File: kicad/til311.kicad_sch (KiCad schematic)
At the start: 32 parts, among them J1 CONN_1x05, J2 CONN_2x07, U1 PIC16F13145

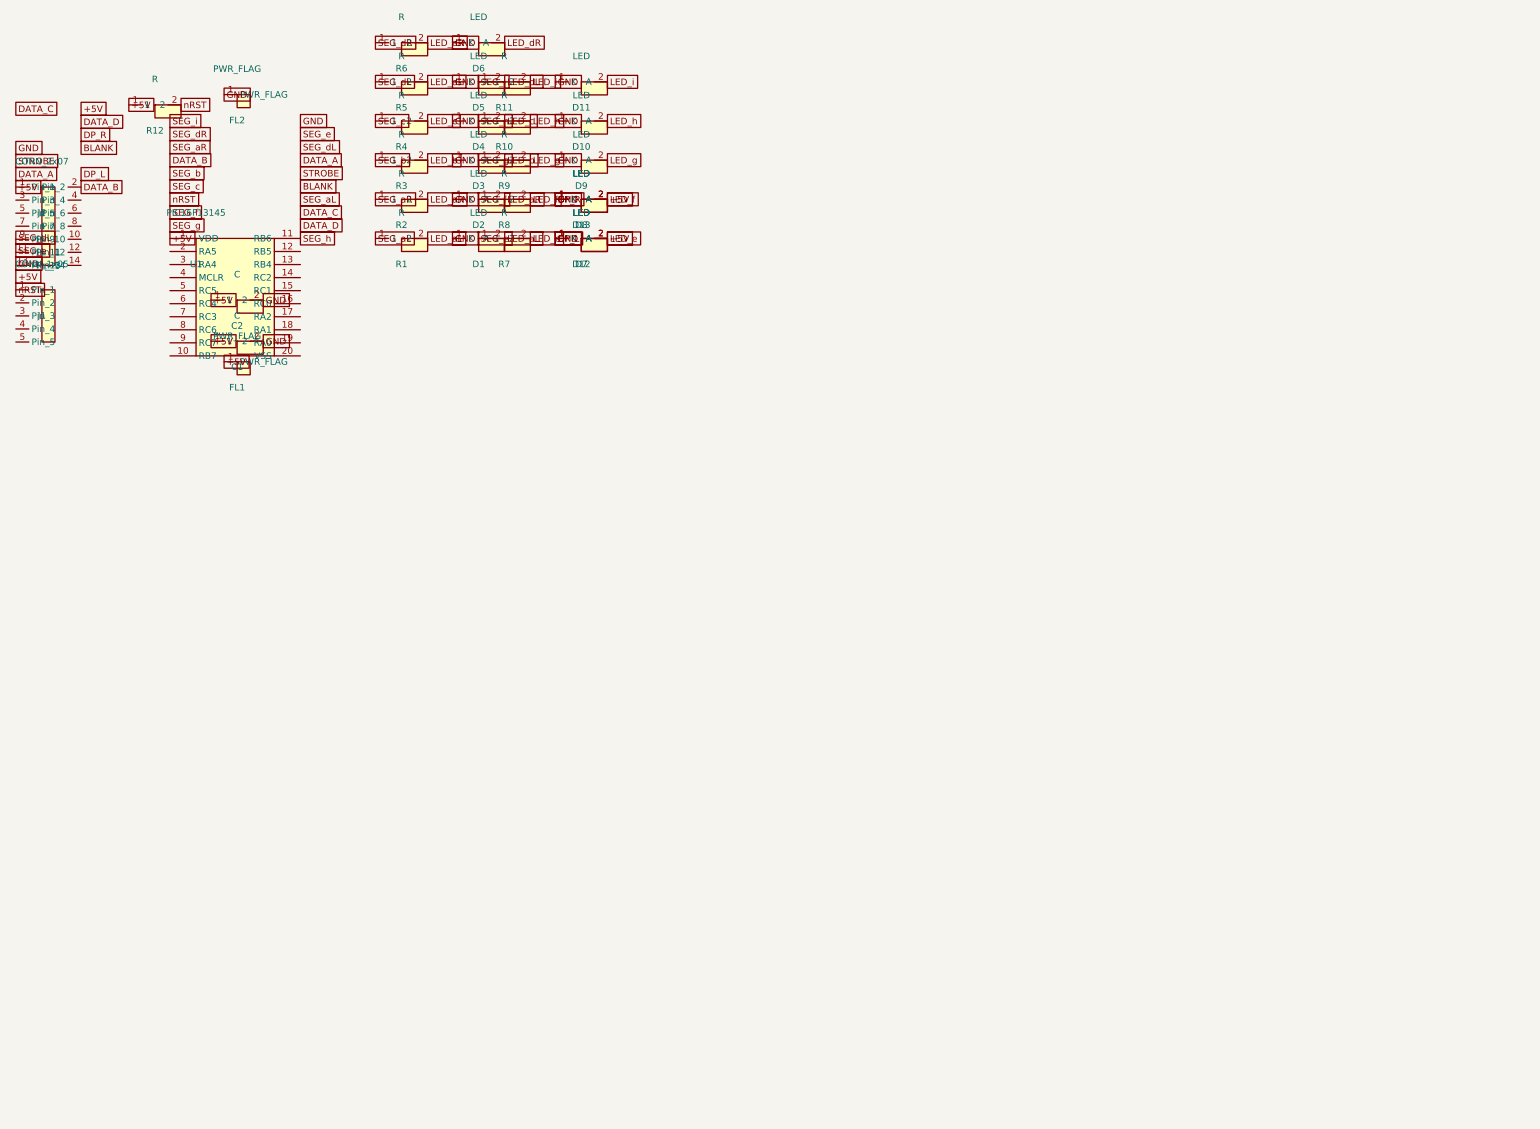
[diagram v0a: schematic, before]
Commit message: kicad: place the schematic components on the page
The hand-generated placement used negative y and near-zero x, which lands
off the A4 sheet (KiCad's page origin is top-left and y grows downward).
Move every component onto the sheet.

Co-Authored-By: Claude <noreply@anthropic.com>
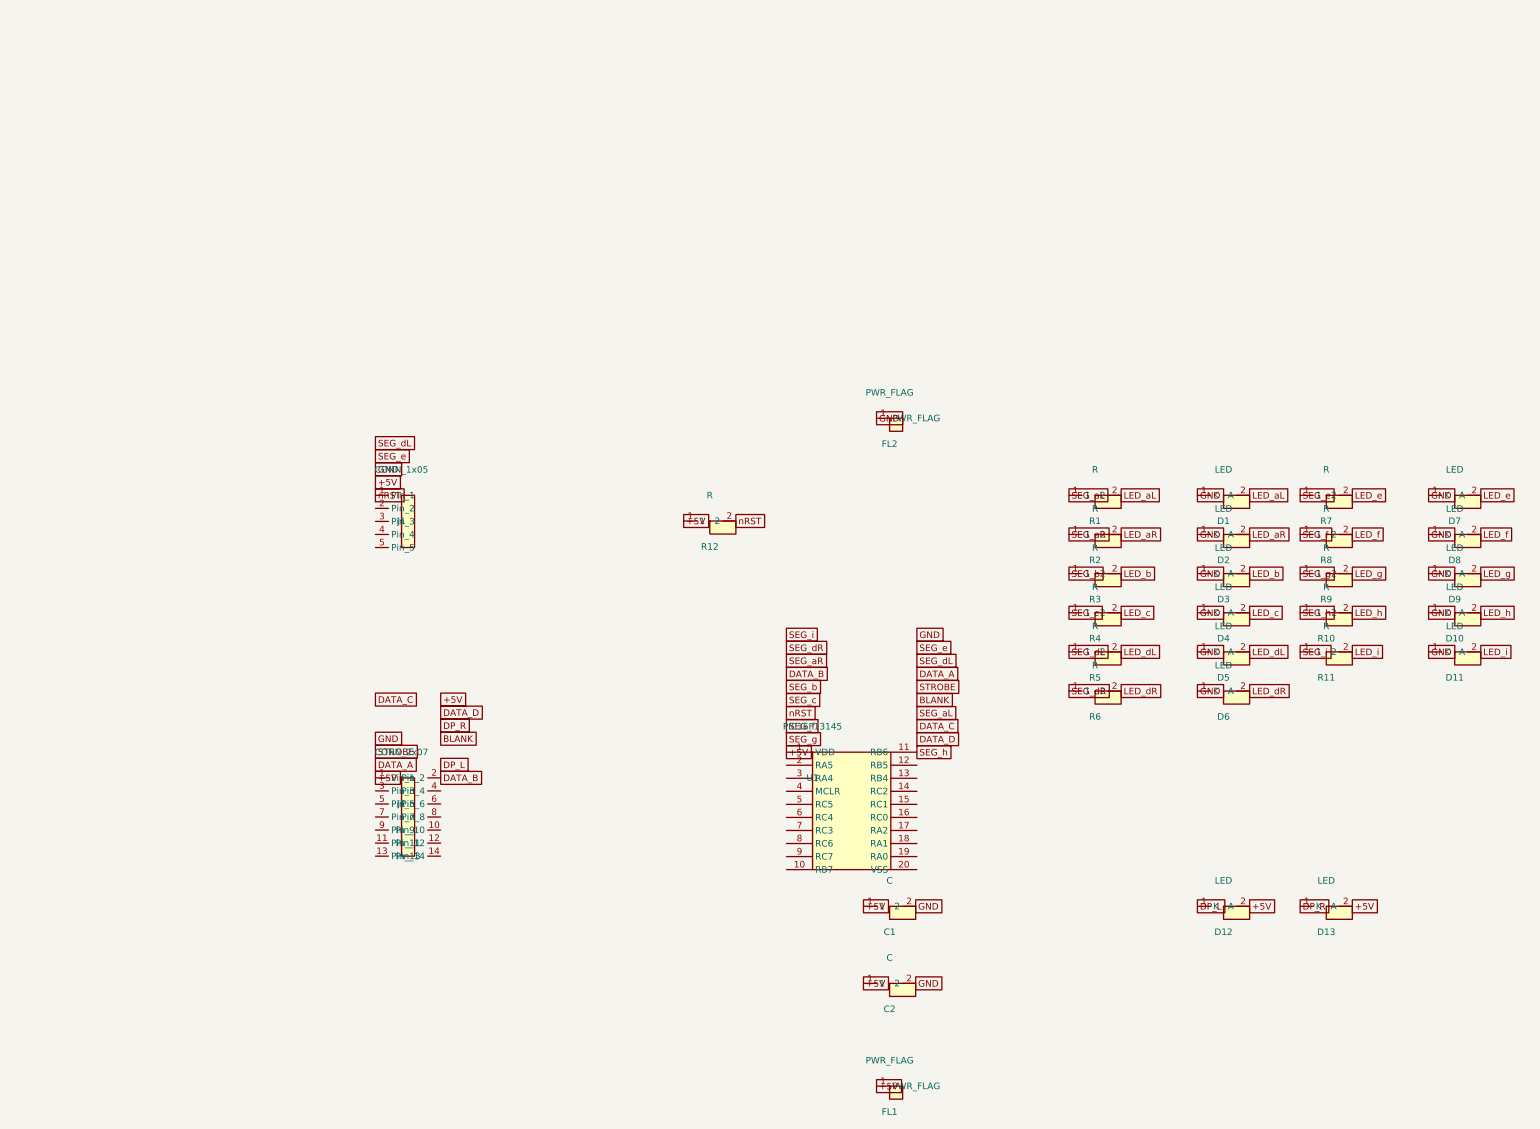
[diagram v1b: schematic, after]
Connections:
- net +5V: no longer D7.2 (A), D8.2 (A), R7.2, R8.2
- net DP_L: no longer C1.2, C2.2, D1.1 (K), D10.1 (K), D11.1 (K), D13.1 (K), D2.1 (K), D3.1 (K), D4.1 (K), D5.1 (K), D6.1 (K), D7.1 (K), D8.1 (K), D9.1 (K), FL2.1 (PWR_FLAG)
- new net DP_R: D13.1 (K)
- new net GND: C1.2, C2.2, D1.1 (K), D10.1 (K), D11.1 (K), D2.1 (K), D3.1 (K), D4.1 (K), D5.1 (K), D6.1 (K), D7.1 (K), D8.1 (K), D9.1 (K), FL2.1 (PWR_FLAG)
- new net LED_e: D7.2 (A), R7.2
- new net LED_f: D8.2 (A), R8.2
